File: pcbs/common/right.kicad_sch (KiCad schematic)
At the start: 89 parts, among them J2 TRS

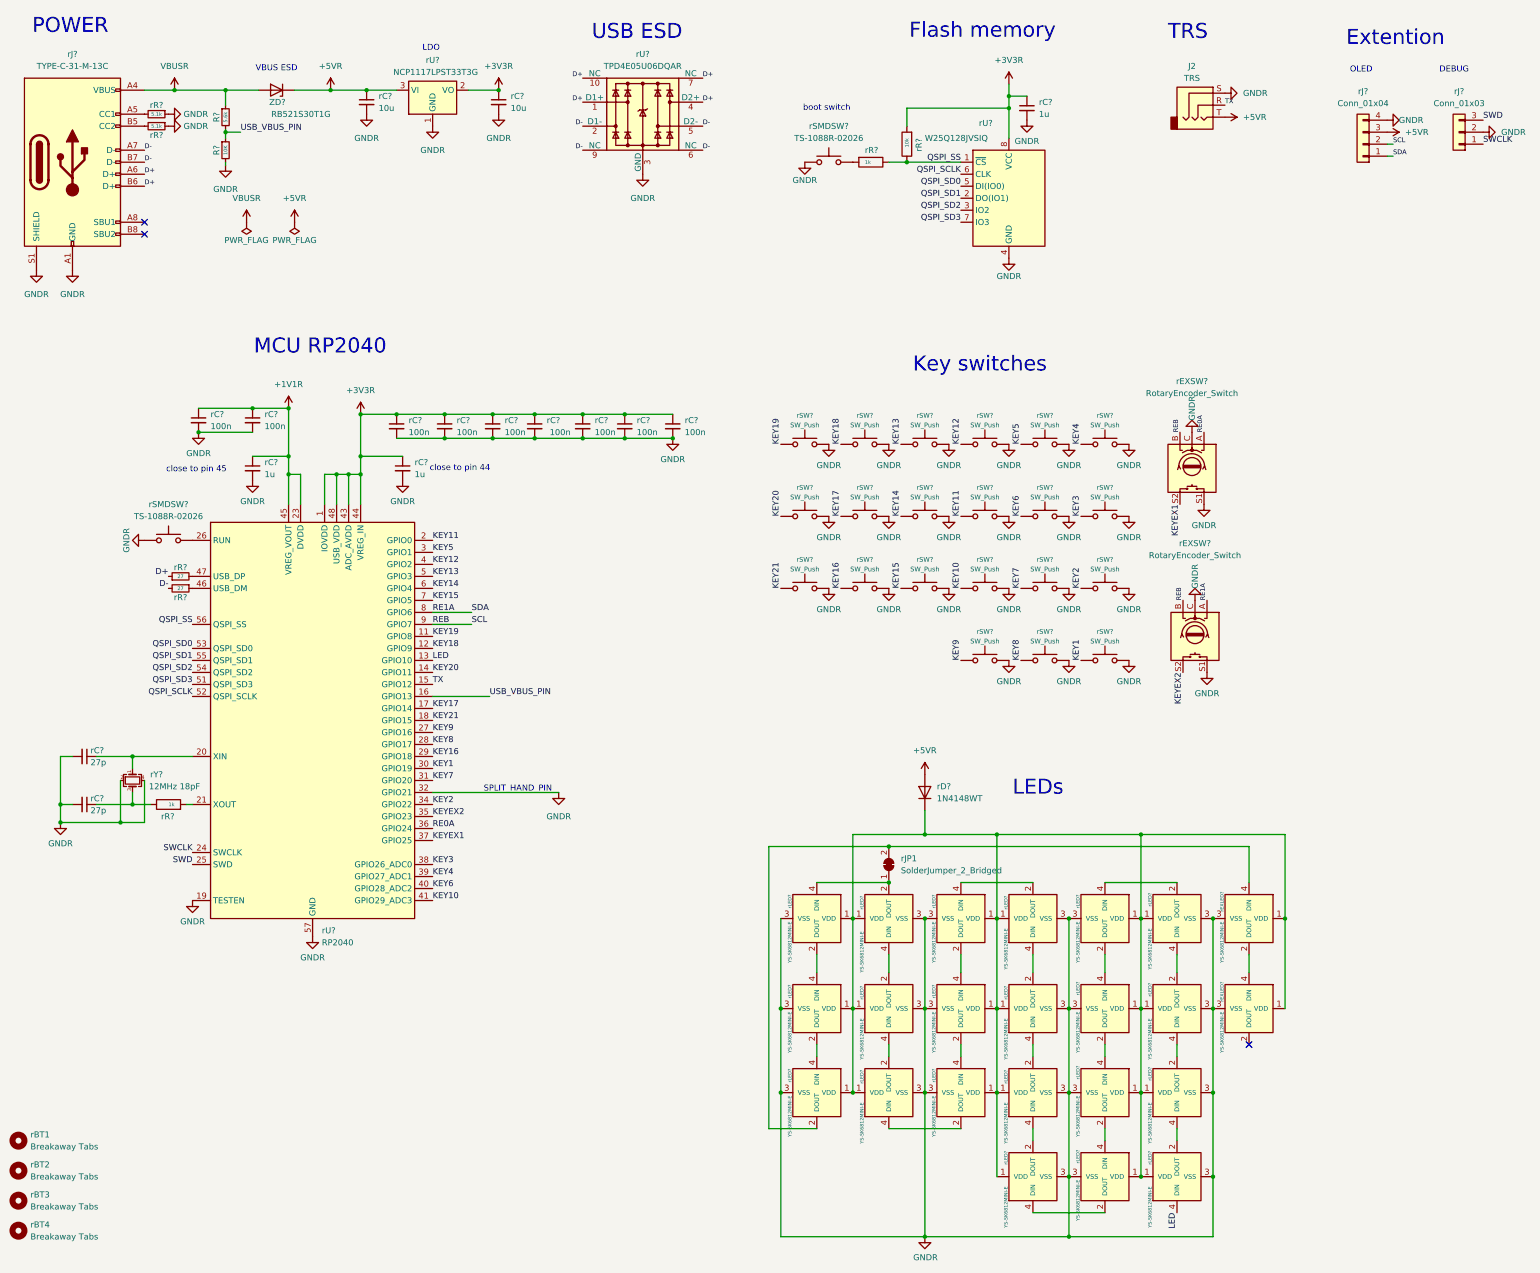
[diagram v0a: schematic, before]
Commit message: Move MCU to the center of the PCB
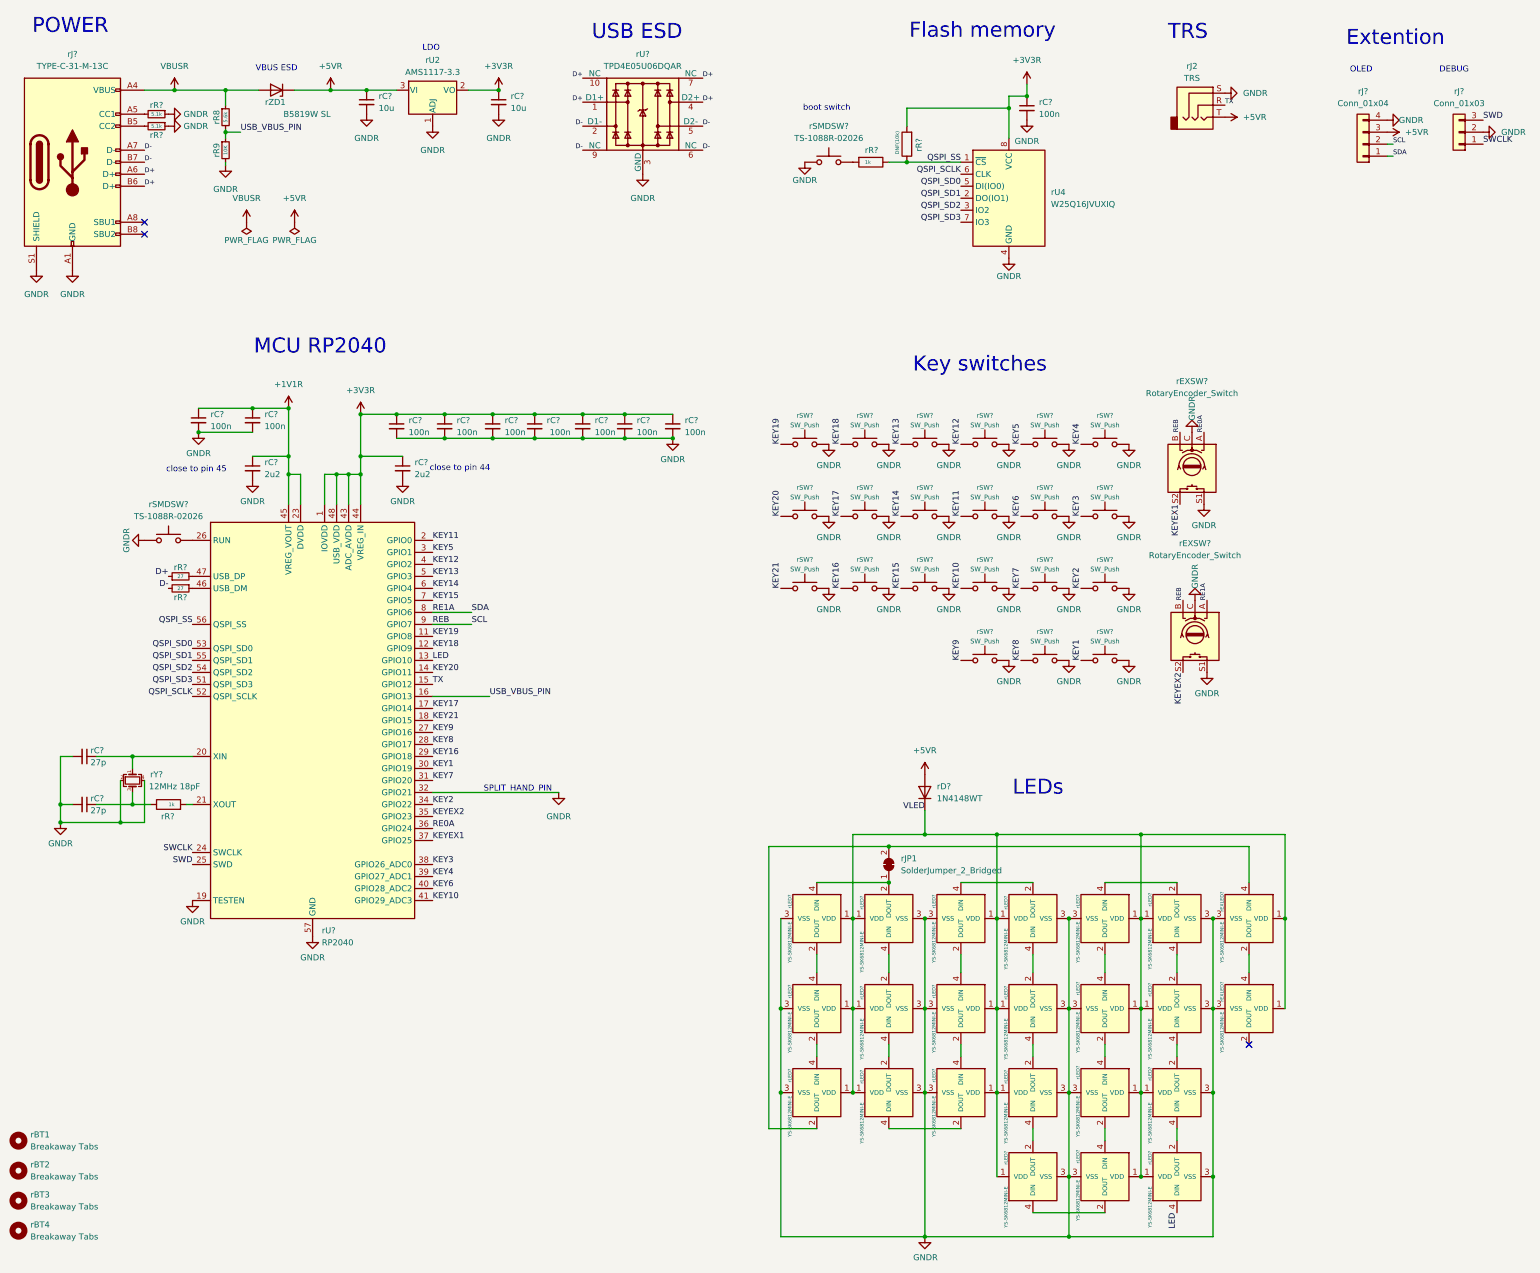
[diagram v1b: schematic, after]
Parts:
- removed rU?: NCP1117LPST33T3G, Package_TO_SOT_SMD:SOT-223-3_TabPin2, symbol Regulator_Linear:NCP1117-3.3_SOT223
- removed rU?: W25Q128JVSIQ, Package_SO:SOIC-8_5.23x5.23mm_P1.27mm, symbol Memory_Flash:W25Q128JVS
- added rU2: AMS1117-3.3, Package_TO_SOT_SMD:SOT-89-3, symbol Regulator_Linear:LM317L_SOT-89
- added rU4: W25Q16JVUXIQ, Package_SON:Winbond_USON-8-1EP_3x2mm_P0.5mm_EP0.2x1.6mm, symbol Memory_Flash:W25Q16JVSS
- rC? (x11): footprint Capacitor_SMD:C_0402_1005Metric -> Capacitor_SMD:C_0201_0603Metric
- rC? (x2): value 1u -> 2u2
- rC? (x2): footprint Capacitor_SMD:C_0402_1005Metric -> Capacitor_SMD:C_0805_2012Metric
- rC?: value 1u -> 100n; footprint Capacitor_SMD:C_0402_1005Metric -> Capacitor_SMD:C_0201_0603Metric
- rD?: footprint Diode_SMD:D_SOD-523 -> Diode_SMD:D_SOD-323
- rJ?: JLCPCB Part # C2848620 -> (none); LCSC (none) -> C2848620
- rR? (x2): footprint Resistor_SMD:R_0402_1005Metric -> Resistor_SMD:R_0201_0603Metric; LCSC (none) -> C25905
- rR?: value 10k -> DNF(10k)
- rR? (x2): footprint Resistor_SMD:R_0402_1005Metric -> Capacitor_SMD:C_0201_0603Metric
- rZD1: renamed from ZD?; value RB521S30T1G -> B5819W SL; footprint Diode_SMD:D_SOD-523 -> Diode_SMD:D_SOD-123; JLCPCB Part # C145179 -> C8598
- gave numbers to parts that had none: 2
- renumbered J2 to rJ2
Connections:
- net +3V3R: now also rU2.2 (VO), rU4.8 (VCC)
- net +5VR: now also rU2.3 (VI)
- net GNDR: now also rU2.1 (ADJ), rU4.4 (GND)
- net QSPI_SCLK: now also rU4.6 (CLK)
- net QSPI_SD0: now also rU4.5 (DI(IO0))
- net QSPI_SD1: now also rU4.2 (DO(IO1))
- net QSPI_SD2: now also rU4.3 (IO2)
- net QSPI_SD3: now also rU4.7 (IO3)
- net QSPI_SS: now also rU4.1 (~{CS})
- net VLED: now reaches rD?.1 (K), rEXLED?.1 (VDD), rEXLED?.1 (VDD), rLED?.1 (VDD), rLED?.1 (VDD), rLED?.1 (VDD), rLED?.1 (VDD), rLED?.1 (VDD), rLED?.1 (VDD), rLED?.1 (VDD), rLED?.1 (VDD), rLED?.1 (VDD), rLED?.1 (VDD), rLED?.1 (VDD), rLED?.1 (VDD), rLED?.1 (VDD), rLED?.1 (VDD), rLED?.1 (VDD), rLED?.1 (VDD), rLED?.1 (VDD), rLED?.1 (VDD), rLED?.1 (VDD), rLED?.1 (VDD), rLED?.1 (VDD)

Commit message: Generate production files
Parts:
- rBT1, rBT2, rBT3, rBT4, rJ? (x2), rJP1: now left out of the parts list
- rC? (x2): LCSC Part # (none) -> C85899
- rC? (x10): LCSC Part # (none) -> C76939
- rC? (x2): value 2u2 -> 1u; LCSC Part # (none) -> C52923
- rC? (x2): LCSC Part # (none) -> C15850
- rD?: value 1N4148WT -> 1N4148W; JLCPCB Part # C232841 -> C2128
- rEXLED? (x2), rLED? (x21): LCSC Part # (none) -> C5149201
- rJ?: LCSC C2848620 -> (none); LCSC Part # (none) -> C2848620
- rR8: LCSC Part # (none) -> C25908
- rR9, rR?: LCSC Part # (none) -> C25744
- rR? (x2): LCSC C25905 -> (none); LCSC Part # (none) -> C270344
- rR? (x2): LCSC Part # (none) -> C11702
- rR? (x2): LCSC Part # (none) -> C270320
- rSW? (x20): footprint kbd:keyswitch_cherrymx_hotswap_1u -> kbd_local:keyswitch_cherrymx_hotswap_1u
- rSW?: footprint kbd:keyswitch_cherrymx_hotswap_1.5u -> kbd_local:keyswitch_cherrymx_hotswap_1.5u

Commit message: Add Corne Chocolate v4.1.1
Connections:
- net GNDR: now also rEXSW?.S2, rEXSW?.S2; no longer rEXSW?.S1, rEXSW?.S1
- net KEYEX1: now also rEXSW?.S1; no longer rEXSW?.S2
- net KEYEX2: now also rEXSW?.S1; no longer rEXSW?.S2
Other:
- moved on the sheet: rEXSW?
